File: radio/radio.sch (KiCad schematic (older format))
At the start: 2 parts

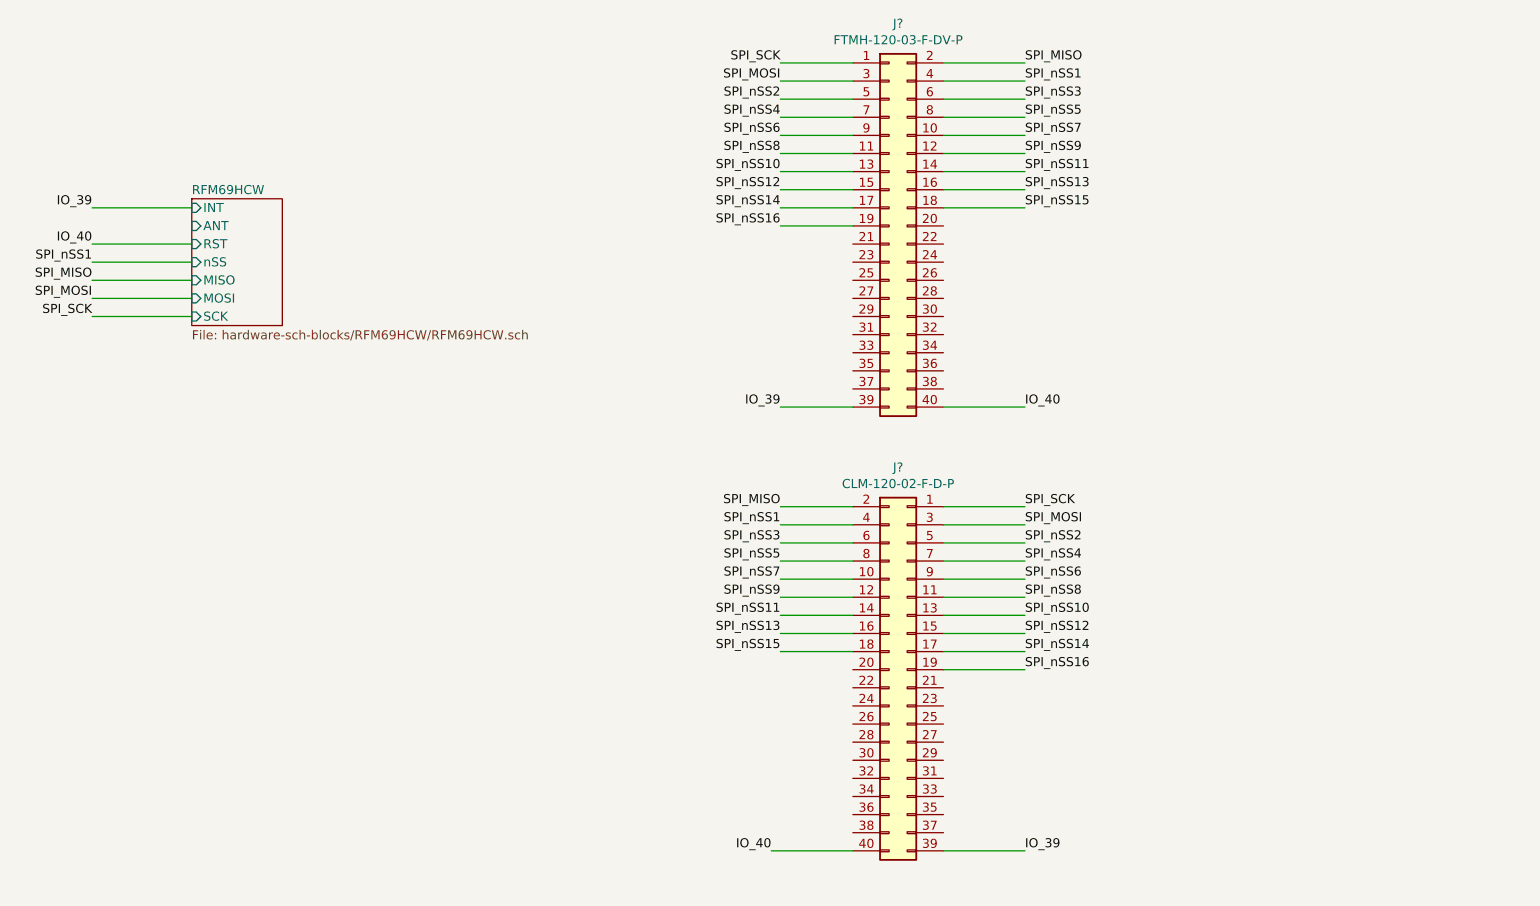
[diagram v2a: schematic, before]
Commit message: update connector pinout on radio
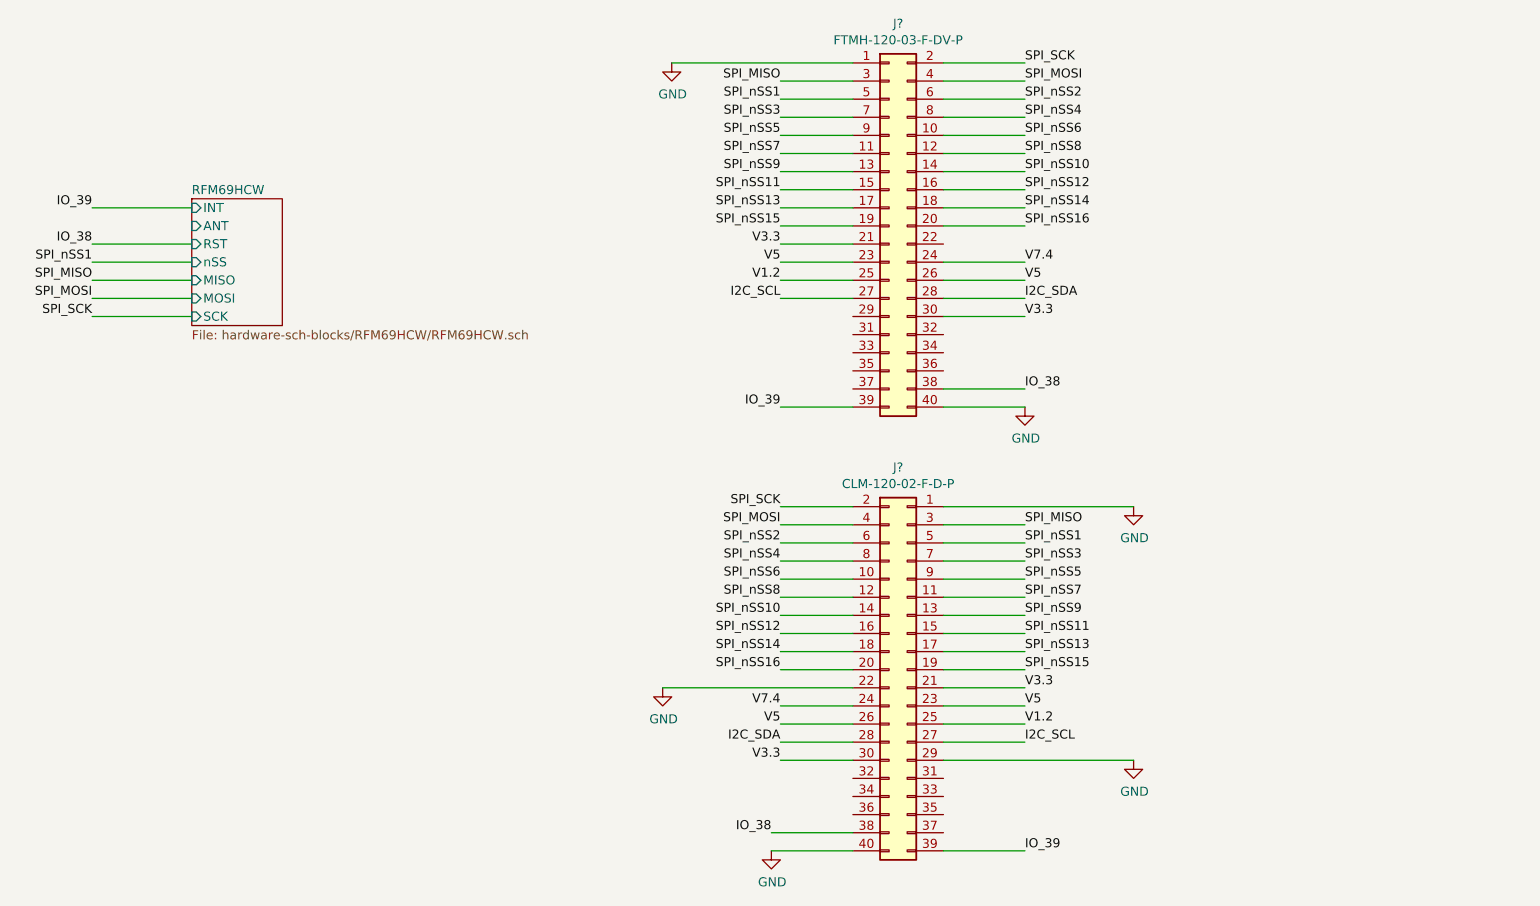
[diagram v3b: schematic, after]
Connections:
- net IO_40 is gone; now on net GND: J?.40 (Pin_40), J?.40 (Pin_40)
- net SPI_MISO: now also J?.3 (Pin_3), J?.3 (Pin_3); no longer J?.2 (Pin_2), J?.2 (Pin_2)
- net SPI_MOSI: now also J?.4 (Pin_4), J?.4 (Pin_4); no longer J?.3 (Pin_3), J?.3 (Pin_3)
- net SPI_SCK: now also J?.2 (Pin_2), J?.2 (Pin_2); no longer J?.1 (Pin_1), J?.1 (Pin_1)
- net SPI_nSS1: now also J?.5 (Pin_5), J?.5 (Pin_5); no longer J?.4 (Pin_4), J?.4 (Pin_4)
- net SPI_nSS10: now also J?.14 (Pin_14), J?.14 (Pin_14); no longer J?.13 (Pin_13), J?.13 (Pin_13)
- net SPI_nSS11: now also J?.15 (Pin_15), J?.15 (Pin_15); no longer J?.14 (Pin_14), J?.14 (Pin_14)
- net SPI_nSS12: now also J?.16 (Pin_16), J?.16 (Pin_16); no longer J?.15 (Pin_15), J?.15 (Pin_15)
- net SPI_nSS13: now also J?.17 (Pin_17), J?.17 (Pin_17); no longer J?.16 (Pin_16), J?.16 (Pin_16)
- net SPI_nSS14: now also J?.18 (Pin_18), J?.18 (Pin_18); no longer J?.17 (Pin_17), J?.17 (Pin_17)
- net SPI_nSS15: now also J?.19 (Pin_19), J?.19 (Pin_19); no longer J?.18 (Pin_18), J?.18 (Pin_18)
- net SPI_nSS16: now also J?.20 (Pin_20), J?.20 (Pin_20); no longer J?.19 (Pin_19), J?.19 (Pin_19)
- net SPI_nSS2: now also J?.6 (Pin_6), J?.6 (Pin_6); no longer J?.5 (Pin_5), J?.5 (Pin_5)
- net SPI_nSS3: now also J?.7 (Pin_7), J?.7 (Pin_7); no longer J?.6 (Pin_6), J?.6 (Pin_6)
- net SPI_nSS4: now also J?.8 (Pin_8), J?.8 (Pin_8); no longer J?.7 (Pin_7), J?.7 (Pin_7)
- net SPI_nSS5: now also J?.9 (Pin_9), J?.9 (Pin_9); no longer J?.8 (Pin_8), J?.8 (Pin_8)
- net SPI_nSS6: now also J?.10 (Pin_10), J?.10 (Pin_10); no longer J?.9 (Pin_9), J?.9 (Pin_9)
- net SPI_nSS7: now also J?.11 (Pin_11), J?.11 (Pin_11); no longer J?.10 (Pin_10), J?.10 (Pin_10)
- net SPI_nSS8: now also J?.12 (Pin_12), J?.12 (Pin_12); no longer J?.11 (Pin_11), J?.11 (Pin_11)
- net SPI_nSS9: now also J?.13 (Pin_13), J?.13 (Pin_13); no longer J?.12 (Pin_12), J?.12 (Pin_12)
- net V3.3: now reaches J?.21 (Pin_21)
- net V3.3: now also J?.21 (Pin_21), J?.30 (Pin_30), J?.30 (Pin_30)
- net V5: now reaches J?.23 (Pin_23)
- net V5: now also J?.23 (Pin_23), J?.26 (Pin_26), J?.26 (Pin_26)
- net V7.4: now reaches J?.24 (Pin_24)
- net V7.4: now also J?.24 (Pin_24)
- net V1.2: now reaches J?.25 (Pin_25)
- net V1.2: now also J?.25 (Pin_25)
- net I2C_SCL: now reaches J?.27 (Pin_27)
- net I2C_SCL: now also J?.27 (Pin_27)
- net I2C_SDA: now reaches J?.28 (Pin_28)
- net I2C_SDA: now also J?.28 (Pin_28)
- net IO_38: now reaches J?.38 (Pin_38)
- net IO_38: now also J?.38 (Pin_38)
- net GND: now reaches J?.22 (Pin_22)
- net GND: now also J?.1 (Pin_1), J?.1 (Pin_1), J?.29 (Pin_29)
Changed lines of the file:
@@
 	2100 2150 2650 2150
 Wire Wire Line
-	6800 2950 7250 2950
-Wire Wire Line
-	6800 3500 7250 3500
+	6800 2850 7250 2850
 Wire Wire Line
 	6800 3600 7250 3600
 Wire Wire Line
-	5850 5400 6300 5400
+	5850 5300 6300 5300
 Wire Wire Line
 	2100 2050 2650 2050
@@
 Wire Wire Line
 	2100 1850 2650 1850
-Wire Wire Line
-	5900 1050 6300 1050
 Wire Wire Line
 	5900 1150 6300 1150
@@
 	5900 3700 6300 3700
 Text Label 5900 3500 2    50   ~ 0
+SPI_SCK
+Text Label 5900 3600 2    50   ~ 0
+SPI_MOSI
+Text Label 5900 3700 2    50   ~ 0
+SPI_nSS2
+Text Label 5900 3800 2    50   ~ 0
+SPI_nSS4
+Text Label 5900 3900 2    50   ~ 0
+SPI_nSS6
+Text Label 5900 4000 2    50   ~ 0
+SPI_nSS8
+Text Label 5900 4100 2    50   ~ 0
+SPI_nSS10
+Text Label 5900 4200 2    50   ~ 0
+SPI_nSS12
+Text Label 5900 4300 2    50   ~ 0
+SPI_nSS14
+Text Label 7250 3700 0    50   ~ 0
+SPI_nSS1
+Text Label 7250 3800 0    50   ~ 0
+SPI_nSS3
+Text Label 7250 3900 0    50   ~ 0
+SPI_nSS5
+Text Label 7250 4000 0    50   ~ 0
+SPI_nSS7
+Text Label 7250 4100 0    50   ~ 0
+SPI_nSS9
+Text Label 7250 4200 0    50   ~ 0
+SPI_nSS11
+Text Label 7250 4300 0    50   ~ 0
+SPI_nSS13
+Text Label 7250 4400 0    50   ~ 0
+SPI_nSS15
+Wire Wire Line
+	5900 3800 6300 3800
+Wire Wire Line
+	5900 3900 6300 3900
+Wire Wire Line
+	5900 4000 6300 4000
+Wire Wire Line
+	5900 4100 6300 4100
+Wire Wire Line
+	5900 4200 6300 4200
+Wire Wire Line
+	5900 4300 6300 4300
+Wire Wire Line
+	6800 3700 7250 3700
+Wire Wire Line
+	6800 3800 7250 3800
+Wire Wire Line
+	6800 3900 7250 3900
+Wire Wire Line
+	6800 4000 7250 4000
+Wire Wire Line
+	6800 4100 7250 4100
+Wire Wire Line
+	6800 4200 7250 4200
+Wire Wire Line
+	6800 4300 7250 4300
+Wire Wire Line
+	6800 4400 7250 4400
+Text Label 7250 3600 0    50   ~ 0
 SPI_MISO
-Text Label 5900 3600 2    50   ~ 0
-SPI_nSS1
-Text Label 5900 3700 2    50   ~ 0
-SPI_nSS3
-Text Label 5900 3800 2    50   ~ 0
-SPI_nSS5
-Text Label 5900 3900 2    50   ~ 0
-SPI_nSS7
-Text Label 5900 4000 2    50   ~ 0
-SPI_nSS9
-Text Label 5900 4100 2    50   ~ 0
-SPI_nSS11
-Text Label 5900 4200 2    50   ~ 0
-SPI_nSS13
-Text Label 5900 4300 2    50   ~ 0
-SPI_nSS15
-Text Label 7250 3700 0    50   ~ 0
-SPI_nSS2
-Text Label 7250 3800 0    50   ~ 0
-SPI_nSS4
-Text Label 7250 3900 0    50   ~ 0
-SPI_nSS6
-Text Label 7250 4000 0    50   ~ 0
-SPI_nSS8
-Text Label 7250 4100 0    50   ~ 0
-SPI_nSS10
-Text Label 7250 4200 0    50   ~ 0
-SPI_nSS12
-Text Label 7250 4300 0    50   ~ 0
-SPI_nSS14
-Text Label 7250 4400 0    50   ~ 0
-SPI_nSS16
-Wire Wire Line
-	5900 3800 6300 3800
-Wire Wire Line
-	5900 3900 6300 3900
-Wire Wire Line
-	5900 4000 6300 4000
-Wire Wire Line
-	5900 4100 6300 4100
-Wire Wire Line
-	5900 4200 6300 4200
-Wire Wire Line
-	5900 4300 6300 4300
-Wire Wire Line
-	6800 3700 7250 3700
-Wire Wire Line
-	6800 3800 7250 3800
-Wire Wire Line
-	6800 3900 7250 3900
-Wire Wire Line
-	6800 4000 7250 4000
-Wire Wire Line
-	6800 4100 7250 4100
-Wire Wire Line
-	6800 4200 7250 4200
-Wire Wire Line
-	6800 4300 7250 4300
-Wire Wire Line
-	6800 4400 7250 4400
-Text Label 7250 3500 0    50   ~ 0
-SPI_SCK
-Text Label 7250 3600 0    50   ~ 0
-SPI_MOSI
 Text Label 7250 5400 0    50   ~ 0
 IO_39
 Text Label 7250 1050 0    50   ~ 0
+SPI_SCK
+Text Label 7250 1150 0    50   ~ 0
+SPI_MOSI
+Text Label 7250 1250 0    50   ~ 0
+SPI_nSS2
+Text Label 7250 1350 0    50   ~ 0
+SPI_nSS4
+Text Label 7250 1450 0    50   ~ 0
+SPI_nSS6
+Text Label 7250 1550 0    50   ~ 0
+SPI_nSS8
+Text Label 7250 1650 0    50   ~ 0
+SPI_nSS10
+Text Label 7250 1750 0    50   ~ 0
+SPI_nSS12
+Text Label 7250 1850 0    50   ~ 0
+SPI_nSS14
+Text Label 7250 2850 0    50   ~ 0
+IO_38
+Text Label 5900 1150 2    50   ~ 0
 SPI_MISO
-Text Label 7250 1150 0    50   ~ 0
-SPI_nSS1
-Text Label 7250 1250 0    50   ~ 0
-SPI_nSS3
-Text Label 7250 1350 0    50   ~ 0
-SPI_nSS5
-Text Label 7250 1450 0    50   ~ 0
-SPI_nSS7
-Text Label 7250 1550 0    50   ~ 0
-SPI_nSS9
-Text Label 7250 1650 0    50   ~ 0
-SPI_nSS11
-Text Label 7250 1750 0    50   ~ 0
-SPI_nSS13
-Text Label 7250 1850 0    50   ~ 0
-SPI_nSS15
-Text Label 7250 2950 0    50   ~ 0
-IO_40
-Text Label 5900 1050 2    50   ~ 0
-SPI_SCK
-Text Label 5900 1150 2    50   ~ 0
-SPI_MOSI
 Text Label 5900 2950 2    50   ~ 0
 IO_39
 Text Label 5900 1250 2    50   ~ 0
-SPI_nSS2
+SPI_nSS1
 Text Label 5900 1350 2    50   ~ 0
-SPI_nSS4
+SPI_nSS3
 Text Label 5900 1450 2    50   ~ 0
-SPI_nSS6
+SPI_nSS5
 Text Label 5900 1550 2    50   ~ 0
-SPI_nSS8
+SPI_nSS7
 Text Label 5900 1650 2    50   ~ 0
-SPI_nSS10
+SPI_nSS9
 Text Label 5900 1750 2    50   ~ 0
-SPI_nSS12
+SPI_nSS11
 Text Label 5900 1850 2    50   ~ 0
-SPI_nSS14
+SPI_nSS13
 Text Label 5900 1950 2    50   ~ 0
-SPI_nSS16
+SPI_nSS15
 Text Label 2100 1850 2    50   ~ 0
 IO_39
 Text Label 2100 2050 2    50   ~ 0
-IO_40
+IO_38
 Text Label 2100 2150 2    50   ~ 0
 SPI_nSS1
@@
 Wire Wire Line
 	6800 1850 7250 1850
-Text Label 5850 5400 2    50   ~ 0
-IO_40
+Text Label 5850 5300 2    50   ~ 0
+IO_38
+Text Label 5900 4400 2    50   ~ 0
+SPI_nSS16
+Wire Wire Line
+	5900 4400 6300 4400
+$Comp
+L power:GND #PWR?
+U 1 1 5E6606DC
+P 7850 3500
+F 0 "#PWR?" H 7850 3250 50  0001 C CNN
+F 1 "GND" H 7855 3327 50  0000 C CNN
+F 2 "" H 7850 3500 50  0001 C CNN
+F 3 "" H 7850 3500 50  0001 C CNN
+	1    7850 3500
+	1    0    0    -1
+$EndComp
+Wire Wire Line
+	6800 3500 7850 3500
+Text Label 7250 1950 0    50   ~ 0
+SPI_nSS16
+Wire Wire Line
+	7250 1950 6800 1950
+$Comp
+L power:GND #PWR?
+U 1 1 5E666581
+P 5300 1050
+F 0 "#PWR?" H 5300 800 50  0001 C CNN
+F 1 "GND" H 5305 877 50  0000 C CNN
+F 2 "" H 5300 1050 50  0001 C CNN
+F 3 "" H 5300 1050 50  0001 C CNN
+	1    5300 1050
+	1    0    0    -1
+$EndComp
+Wire Wire Line
+	5300 1050 6300 1050
+$Comp
+L power:GND #PWR?
+U 1 1 5E667F20
+P 5850 5400
+F 0 "#PWR?" H 5850 5150 50  0001 C CNN
+F 1 "GND" H 5855 5227 50  0000 C CNN
+F 2 "" H 5850 5400 50  0001 C CNN
+F 3 "" H 5850 5400 50  0001 C CNN
+	1    5850 5400
+	1    0    0    -1
+$EndComp
+Wire Wire Line
+	5850 5400 6300 5400
+$Comp
+L power:GND #PWR?
+U 1 1 5E669858
+P 7250 2950
+F 0 "#PWR?" H 7250 2700 50  0001 C CNN
+F 1 "GND" H 7255 2777 50  0000 C CNN
+F 2 "" H 7250 2950 50  0001 C CNN
+F 3 "" H 7250 2950 50  0001 C CNN
+	1    7250 2950
+	1    0    0    -1
+$EndComp
+Wire Wire Line
+	7250 2950 6800 2950
+Text Label 5900 2050 2    50   ~ 0
+V3.3
+Wire Wire Line
+	5900 2050 6300 2050
+Text Label 5900 2150 2    50   ~ 0
+V5
+Text Label 5900 2250 2    50   ~ 0
+V1.2
+Text Label 5900 2350 2    50   ~ 0
+I2C_SCL
+Text Label 5900 4600 2    50   ~ 0
+V7.4
+Text Label 5900 4700 2    50   ~ 0
+V5
+Text Label 5900 4800 2    50   ~ 0
+I2C_SDA
+Text Label 5900 4900 2    50   ~ 0
+V3.3
+Text Label 7250 2150 0    50   ~ 0
+V7.4
+Text Label 7250 2250 0    50   ~ 0
+V5
+Text Label 7250 2350 0    50   ~ 0
+I2C_SDA
+Text Label 7250 2450 0    50   ~ 0
+V3.3
+Wire Wire Line
+	5900 2150 6300 2150
+Wire Wire Line
+	5900 2250 6300 2250
+Wire Wire Line
+	6300 2350 5900 2350
+Wire Wire Line
+	7250 2150 6800 2150
+Wire Wire Line
+	6800 2250 7250 2250
+Wire Wire Line
+	7250 2350 6800 2350
+Wire Wire Line
+	6800 2450 7250 2450
+Wire Wire Line
+	5900 4600 6300 4600
+Wire Wire Line
+	5900 4700 6300 4700
+Wire Wire Line
+	5900 4800 6300 4800
+Wire Wire Line
+	5900 4900 6300 4900
+Text Label 7250 4500 0    50   ~ 0
+V3.3
+Text Label 7250 4600 0    50   ~ 0
+V5
+Text Label 7250 4700 0    50   ~ 0
+V1.2
+Text Label 7250 4800 0    50   ~ 0
+I2C_SCL
+Wire Wire Line
+	6800 4500 7250 4500
+Wire Wire Line
+	6800 4600 7250 4600
+Wire Wire Line
+	6800 4700 7250 4700
+Wire Wire Line
+	6800 4800 7250 4800
+$Comp
+L power:GND #PWR?
+U 1 1 5E68EBE3
+P 7850 4900
+F 0 "#PWR?" H 7850 4650 50  0001 C CNN
+F 1 "GND" H 7855 4727 50  0000 C CNN
+F 2 "" H 7850 4900 50  0001 C CNN
+F 3 "" H 7850 4900 50  0001 C CNN
+	1    7850 4900
+	1    0    0    -1
+$EndComp
+$Comp
+L power:GND #PWR?
+U 1 1 5E68EDF9
+P 5250 4500
+F 0 "#PWR?" H 5250 4250 50  0001 C CNN
+F 1 "GND" H 5255 4327 50  0000 C CNN
+F 2 "" H 5250 4500 50  0001 C CNN
+F 3 "" H 5250 4500 50  0001 C CNN
+	1    5250 4500
+	1    0    0    -1
+$EndComp
+Wire Wire Line
+	5250 4500 6300 4500
+Wire Wire Line
+	6800 4900 7850 4900
 $EndSCHEMATC

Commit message: trying to push radio again
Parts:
- removed J?: FTMH-120-03-F-DV-P, symbol star-common-lib:FTMH-120-03-F-DV-P
- removed J?: CLM-120-02-F-D-P, symbol star-common-lib:CLM-120-02-F-D-P
